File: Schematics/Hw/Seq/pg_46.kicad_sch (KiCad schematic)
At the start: 9 parts, among them U4701 F138, U4702 F194, U4703 F194, U4704 F02, U4705 F258, U4706 F258, U4707 F258, U4708 F258, U4709 F04

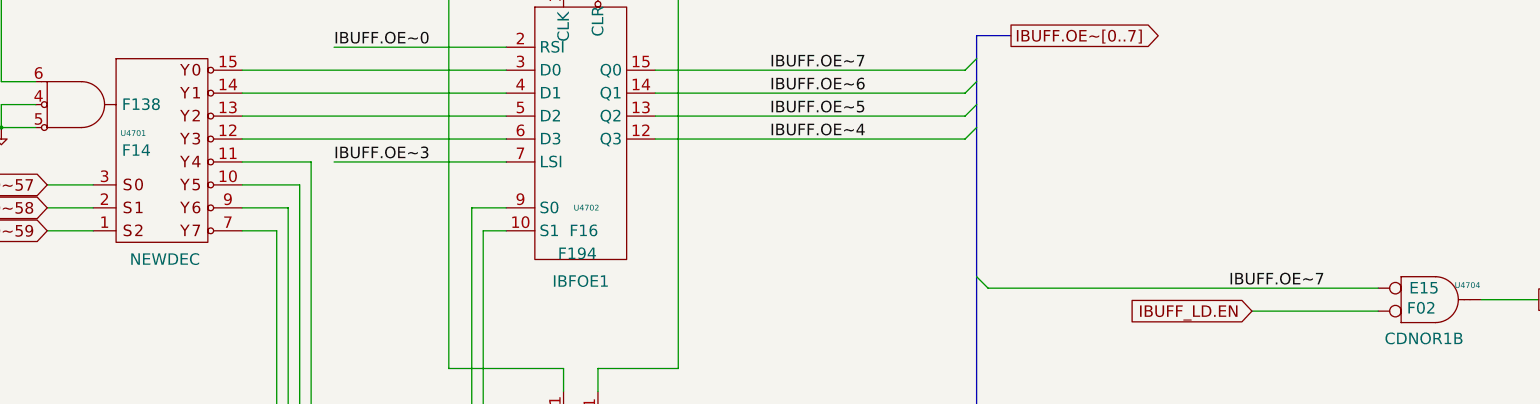
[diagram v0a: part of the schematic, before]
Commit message: Upgrade to KiCad9
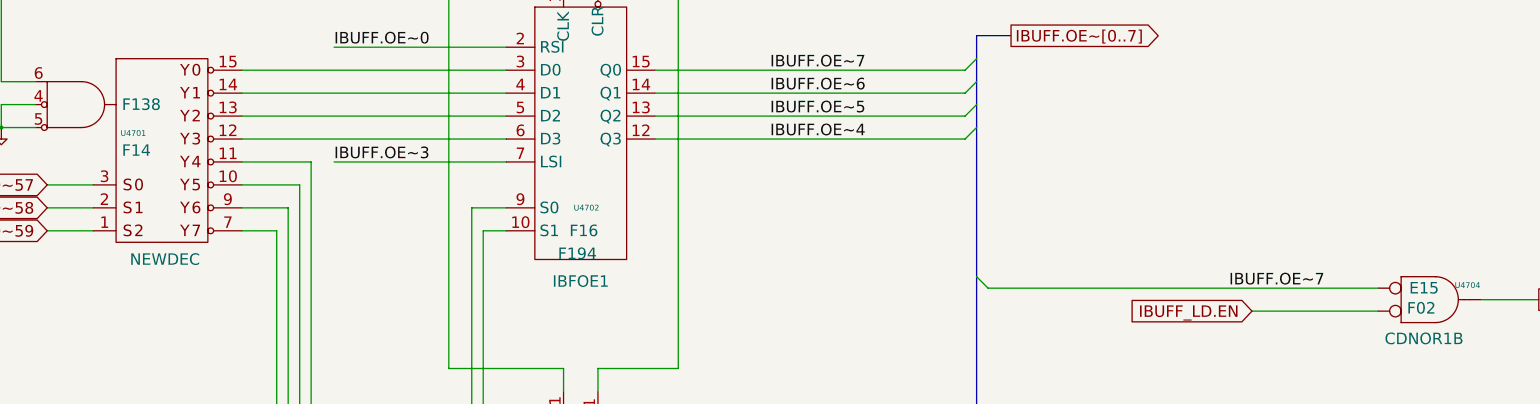
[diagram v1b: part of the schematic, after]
